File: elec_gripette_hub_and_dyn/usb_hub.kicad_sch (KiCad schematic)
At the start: 26 parts, among them J1 pico4, J3 Pogo-pin, J6 Pogo-pin, U1 FE1.1s_24-Pin_WQFN, U2 24C02S, Y1 12MHz

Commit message: [update] sch reviewed by Claude
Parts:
- added C21: 100n, Capacitor_SMD:C_0603_1608Metric, symbol Device:C_Small
- added D3: SP0503BAHT, Package_TO_SOT_SMD:SOT-143, symbol Power_Protection:SP0503BAHT
- J3, J6: footprint LCSC_parts_lib:SMD_BD1,2.0-L1.2-pogo-pin -> LCSC_parts_lib:CONN-TH_YZ95315064P-01_pogo; LCSC Part C5157386 -> C5157245
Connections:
- net +5V: now also C21.2
- net DM+: now also D3.3 (K)
- net DM-: now also D3.2 (K)
- net GND: now also C21.1, D3.1 (A)
- net at J1.2 (Pin_2), R2.1: now also D3.4 (K)
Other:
- note added: "(internaly generated by the USB hub)"

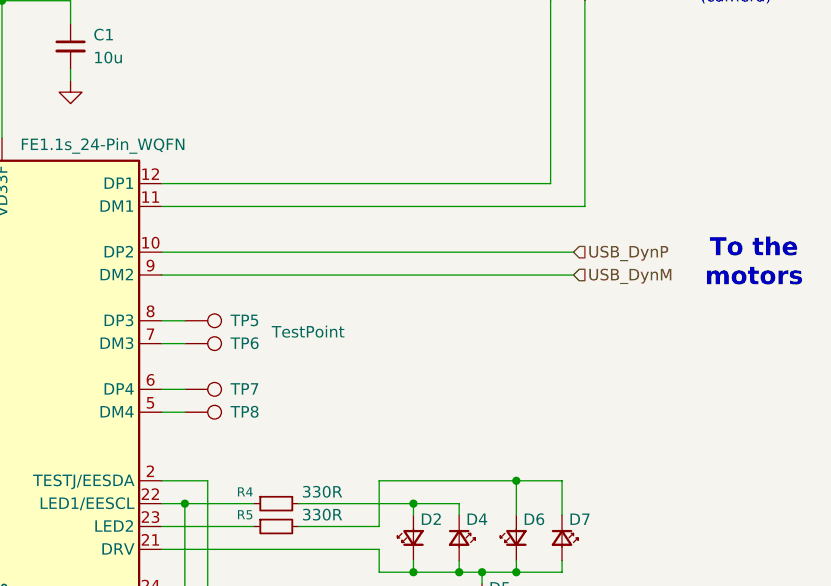
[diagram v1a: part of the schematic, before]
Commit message: [update] Gripette hub routed
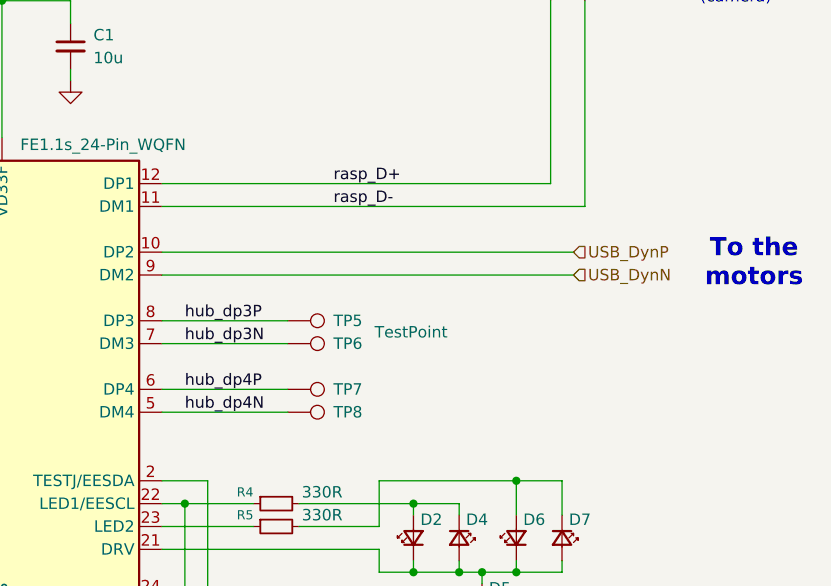
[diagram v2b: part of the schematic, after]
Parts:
- J1: footprint Connector_Molex:Molex_PicoBlade_53048-0410_1x04_P1.25mm_Horizontal -> Connector_Molex:Molex_PicoBlade_53047-0410_1x04_P1.25mm_Vertical; LCSC Part C588275 -> (none)
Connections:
- net rasp_D-: now reaches J6.1, U1.11 (DM1)
- net hub_dp4P: now reaches TP7.1, U1.6 (DP4)
- net hub_dp3N: now reaches TP6.1, U1.7 (DM3)
- net hub_dp4N: now reaches TP8.1, U1.5 (DM4)
- net hub_dp3P: now reaches TP5.1, U1.8 (DP3)
- net rasp_D+: now reaches J3.1, U1.12 (DP1)
- net USB_DynM renamed USB_DynN
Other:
- moved on the sheet: TP5, TP6, TP7, TP8
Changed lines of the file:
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@@
 	(wire
 		(pts
+			(xy 217.17 135.89) (xy 231.14 135.89)
+		)
+		(stroke
+			(width 0)
+			(type default)
+		)
+	)
+	(wire
+		(pts
 			(xy 219.71 200.66) (xy 219.71 146.05)
 		)
@@
 	(wire
 		(pts
-			(xy 130.81 125.73) (xy 130.81 130.81)
+			(xy 217.17 128.27) (xy 231.14 128.27)
 		)
 		(stroke
@@
 	(wire
 		(pts
-			(xy 256.54 152.4) (xy 256.54 153.67)
+			(xy 217.17 133.35) (xy 231.14 133.35)
 		)
 		(stroke
@@
 	(wire
 		(pts
-			(xy 217.17 146.05) (xy 219.71 146.05)
+			(xy 130.81 125.73) (xy 130.81 130.81)
 		)
 		(stroke
@@
 	(wire
 		(pts
-			(xy 260.35 90.17) (xy 260.35 110.49)
+			(xy 256.54 152.4) (xy 256.54 153.67)
 		)
 		(stroke
@@
 	(wire
 		(pts
-			(xy 130.81 125.73) (xy 130.81 115.57)
+			(xy 217.17 146.05) (xy 219.71 146.05)
 		)
 		(stroke
@@
 	(wire
 		(pts
-			(xy 170.18 97.79) (xy 170.18 96.52)
+			(xy 260.35 90.17) (xy 260.35 110.49)
 		)
 		(stroke
@@
 	(wire
 		(pts
-			(xy 179.07 163.83) (xy 179.07 165.1)
+			(xy 130.81 125.73) (xy 130.81 115.57)
 		)
 		(stroke
@@
 	(wire
 		(pts
-			(xy 219.71 133.35) (xy 217.17 133.35)
+			(xy 170.18 97.79) (xy 170.18 96.52)
 		)
 		(stroke
@@
 	(wire
 		(pts
-			(xy 250.19 153.67) (xy 252.73 153.67)
+			(xy 179.07 163.83) (xy 179.07 165.1)
 		)
 		(stroke
@@
 	(wire
 		(pts
-			(xy 245.11 146.05) (xy 245.11 147.32)
+			(xy 250.19 153.67) (xy 252.73 153.67)
 		)
 		(stroke
@@
 	(wire
 		(pts
-			(xy 232.41 146.05) (xy 245.11 146.05)
+			(xy 245.11 146.05) (xy 245.11 147.32)
 		)
 		(stroke
@@
 	(wire
 		(pts
-			(xy 245.11 203.2) (xy 237.49 203.2)
+			(xy 232.41 146.05) (xy 245.11 146.05)
 		)
 		(stroke
@@
 	(wire
 		(pts
-			(xy 194.31 90.17) (xy 194.31 105.41)
+			(xy 245.11 203.2) (xy 237.49 203.2)
 		)
 		(stroke
@@
 	(wire
 		(pts
-			(xy 128.27 118.11) (xy 181.61 118.11)
+			(xy 194.31 90.17) (xy 194.31 105.41)
 		)
 		(stroke
@@
 	(wire
 		(pts
-			(xy 252.73 166.37) (xy 252.73 167.64)
+			(xy 128.27 118.11) (xy 181.61 118.11)
 		)
 		(stroke
@@
 	(wire
 		(pts
-			(xy 241.3 153.67) (xy 245.11 153.67)
+			(xy 252.73 166.37) (xy 252.73 167.64)
 		)
 		(stroke
@@
 	(wire
 		(pts
-			(xy 219.71 135.89) (xy 217.17 135.89)
+			(xy 241.3 153.67) (xy 245.11 153.67)
 		)
 		(stroke
@@
 	(wire
 		(pts
-			(xy 219.71 128.27) (xy 217.17 128.27)
-		)
-		(stroke
-			(width 0)
-			(type default)
-		)
-	)
-	(wire
-		(pts
-			(xy 219.71 125.73) (xy 217.17 125.73)
+			(xy 217.17 125.73) (xy 231.14 125.73)
 		)
 		(stroke
@@
 		)
 	)
+	(label "rasp_D+"
+		(at 236.22 110.49 0)
+		(effects
+			(font
+				(size 1.27 1.27)
+			)
+			(justify left bottom)
+		)
+	)
+	(label "hub_dp3N"
+		(at 219.71 128.27 0)
+		(effects
+			(font
+				(size 1.27 1.27)
+			)
+			(justify left bottom)
+		)
+	)
+	(label "hub_dp4N"
+		(at 219.71 135.89 0)
+		(effects
+			(font
+				(size 1.27 1.27)
+			)
+			(justify left bottom)
+		)
+	)
 	(label "DM-"
 		(at 147.32 118.11 180)
@@
 		)
 	)
-	(hierarchical_label "USB_DynM"
+	(label "rasp_D-"
+		(at 236.22 113.03 0)
+		(effects
+			(font
+				(size 1.27 1.27)
+			)
+			(justify left bottom)
+		)
+	)
+	(label "hub_dp4P"
+		(at 219.71 133.35 0)
+		(effects
+			(font
+				(size 1.27 1.27)
+			)
+			(justify left bottom)
+		)
+	)
+	(label "hub_dp3P"
+		(at 219.71 125.73 0)
+		(effects
+			(font
+				(size 1.27 1.27)
+			)
+			(justify left bottom)
+		)
+	)
+	(hierarchical_label "USB_DynN"
 		(shape input)
 		(at 262.89 120.65 0)
@@
 			)
 		)
-		(property "Footprint" "Connector_Molex:Molex_PicoBlade_53048-0410_1x04_P1.25mm_Horizontal"
+		(property "Footprint" "Connector_Molex:Molex_PicoBlade_53047-0410_1x04_P1.25mm_Vertical"
 			(at 110.49 128.27 0)
 			(effects
@@
 			)
 		)
-		(property "LCSC Part" "C588275"
+		(property "LCSC Part" ""
 			(at 110.49 128.27 0)
 			(effects
@@
 	(symbol
 		(lib_id "Connector:TestPoint")
-		(at 219.71 133.35 270)
+		(at 231.14 133.35 270)
 		(unit 1)
 		(exclude_from_sim no)
@@
 		(fields_autoplaced yes)
 		(property "Reference" "TP7"
-			(at 224.79 133.3499 90)
+			(at 236.22 133.3499 90)
 			(effects
 				(font
@@
 		)
 		(property "Value" "TestPoint"
-			(at 224.79 134.6199 90)
+			(at 236.22 134.6199 90)
 			(effects
 				(font
@@
 		)
 		(property "Footprint" "TestPoint:TestPoint_Pad_D1.0mm"
-			(at 219.71 138.43 0)
+			(at 231.14 138.43 0)
 			(effects
 				(font
@@
 		)
 		(property "Datasheet" "~"
-			(at 219.71 138.43 0)
+			(at 231.14 138.43 0)
 			(effects
 				(font
@@
 		)
 		(property "Description" "test point"
-			(at 219.71 133.35 0)
+			(at 231.14 133.35 0)
 			(effects
 				(font
@@
 	(symbol
 		(lib_id "Connector:TestPoint")
-		(at 219.71 128.27 270)
+		(at 231.14 128.27 270)
 		(unit 1)
 		(exclude_from_sim no)
@@
 		(fields_autoplaced yes)
 		(property "Reference" "TP6"
-			(at 224.79 128.2699 90)
+			(at 236.22 128.2699 90)
 			(effects
 				(font
@@
 		)
 		(property "Value" "TestPoint"
-			(at 224.79 129.5399 90)
+			(at 236.22 129.5399 90)
 			(effects
 				(font
@@
 		)
 		(property "Footprint" "TestPoint:TestPoint_Pad_D1.0mm"
-			(at 219.71 133.35 0)
+			(at 231.14 133.35 0)
 			(effects
 				(font
@@
 		)
 		(property "Datasheet" "~"
-			(at 219.71 133.35 0)
+			(at 231.14 133.35 0)
 			(effects
 				(font
@@
 		)
 		(property "Description" "test point"
-			(at 219.71 128.27 0)
+			(at 231.14 128.27 0)
 			(effects
 				(font
@@
 	(symbol
 		(lib_id "Connector:TestPoint")
-		(at 219.71 135.89 270)
+		(at 231.14 135.89 270)
 		(unit 1)
 		(exclude_from_sim no)
@@
 		(fields_autoplaced yes)
 		(property "Reference" "TP8"
-			(at 224.79 135.8899 90)
+			(at 236.22 135.8899 90)
 			(effects
 				(font
@@
 		)
 		(property "Value" "TestPoint"
-			(at 224.79 137.1599 90)
+			(at 236.22 137.1599 90)
 			(effects
 				(font
@@
 		)
 		(property "Footprint" "TestPoint:TestPoint_Pad_D1.0mm"
-			(at 219.71 140.97 0)
+			(at 231.14 140.97 0)
 			(effects
 				(font
@@
 		)
 		(property "Datasheet" "~"
-			(at 219.71 140.97 0)
+			(at 231.14 140.97 0)
 			(effects
 				(font
@@
 		)
 		(property "Description" "test point"
-			(at 219.71 135.89 0)
+			(at 231.14 135.89 0)
 			(effects
 				(font
@@
 	(symbol
 		(lib_id "Connector:TestPoint")
-		(at 219.71 125.73 270)
+		(at 231.14 125.73 270)
 		(unit 1)
 		(exclude_from_sim no)
@@
 		(dnp no)
 		(property "Reference" "TP5"
-			(at 224.79 125.73 90)
+			(at 236.22 125.73 90)
 			(effects
 				(font
@@
 		)
 		(property "Value" "TestPoint"
-			(at 229.362 127 90)
+			(at 240.792 127 90)
 			(effects
 				(font
@@
 		)
 		(property "Footprint" "TestPoint:TestPoint_Pad_D1.0mm"
-			(at 219.71 130.81 0)
+			(at 231.14 130.81 0)
 			(effects
 				(font
@@
 		)
 		(property "Datasheet" "~"
-			(at 219.71 130.81 0)
+			(at 231.14 130.81 0)
 			(effects
 				(font
@@
 		)
 		(property "Description" "test point"
-			(at 219.71 125.73 0)
+			(at 231.14 125.73 0)
 			(effects
 				(font

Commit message: [uptate] Gripette hub ok for JLC
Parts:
- D2, D6: FT Rotation Offset (none) -> 180
- J1: FT Rotation Offset (none) -> 180; LCSC Part (none) -> C504989
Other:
- company: Pollen Robotics / Hugging Face -> Pollen Robotics/HF
- title: elec_maroilles -> Grippette - USB hub and Dynamixel device
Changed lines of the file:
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@@
 	(paper "A3")
 	(title_block
-		(title "elec_maroilles")
-		(date "2026-02-02")
-		(rev "B1")
-		(company "Pollen Robotics / Hugging Face")
+		(title "Grippette - USB hub and Dynamixel device")
+		(date "2026-04-16")
+		(rev "A1")
+		(company "Pollen Robotics/HF")
 	)
 	(text "To the\nmotors"
@@
 			)
 		)
-		(property "LCSC Part" ""
+		(property "LCSC Part" "C504989"
+			(at 110.49 128.27 0)
+			(effects
+				(font
+					(size 1.27 1.27)
+				)
+				(hide yes)
+			)
+		)
+		(property "FT Rotation Offset" "180"
 			(at 110.49 128.27 0)
 			(effects
@@
 			)
 		)
-		(property "FT Rotation Offset" ""
+		(property "FT Rotation Offset" "180"
 			(at 256.54 149.86 90)
 			(effects
@@
 			)
 		)
-		(property "FT Rotation Offset" ""
+		(property "FT Rotation Offset" "180"
 			(at 245.11 149.86 90)
 			(effects

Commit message: [update] Added error to gripette, going to B1
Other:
- note added: "hub active/suspend indicator"
- note added: "port 1 indicator"
- note added: "port 2 indicator"
- note added: "port 3 indicator"
- note added: "port 4 indicator"
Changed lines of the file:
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@@
+		)
+	)
+	(text "port 4 indicator"
+		(exclude_from_sim no)
+		(at 258.318 138.684 90)
+		(effects
+			(font
+				(size 1.27 1.27)
+			)
 		)
 	)
@@
 			)
 			(justify left)
+		)
+	)
+	(text "port 2 indicator"
+		(exclude_from_sim no)
+		(at 263.906 138.938 90)
+		(effects
+			(font
+				(size 1.27 1.27)
+			)
+		)
+	)
+	(text "port 3 indicator"
+		(exclude_from_sim no)
+		(at 246.888 138.176 90)
+		(effects
+			(font
+				(size 1.27 1.27)
+			)
 		)
 	)
@@
 		(effects
 			(font
+				(size 1.27 1.27)
+			)
+		)
+	)
+	(text "port 1 indicator"
+		(exclude_from_sim no)
+		(at 251.968 138.684 90)
+		(effects
+			(font
+				(size 1.27 1.27)
+			)
+		)
+	)
+	(text "hub active/suspend indicator"
+		(exclude_from_sim no)
+		(at 271.018 157.734 0)
+		(effects
+			(font

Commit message: [update] SCH B1-RC1
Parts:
- added C22: 100n, Capacitor_SMD:C_0603_1608Metric, symbol Device:C_Small
- added J10: Pogo-pin 2A, LCSC_parts_lib:CONN-TH_YZ08415060P-02_pogo, symbol Library_Pollen:pogo-pin
- added R23: DNP - 0R, Resistor_SMD:R_0402_1005Metric, symbol Device:R_Small
- D2, D6: FT Rotation Offset 180 -> (none); LCSC Part C19171301 -> C7429915
- D4, D7: LCSC Part C84263 -> C7429915
- D5: LCSC Part C7429915 -> C19171301
- J3, J6: value Pogo-pin -> Pogo-pin 4mm
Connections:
- net +3V3: now also C22.2
- net GND: now also C22.1
- net at R1.2, U1.16 (~{XRSTJ}): now also R23.1
- new net: J10.1, R23.2
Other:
- note added: "Reseting the hub from the rasp"
- moved on the sheet: C1

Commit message: [update] SCH + PCB B1-RC1
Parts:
- J10: value Pogo-pin 2A -> Pogo-pin 4mm; footprint LCSC_parts_lib:CONN-TH_YZ08415060P-02_pogo -> LCSC_parts_lib:CONN-TH_YZ95315064P-01_pogo; LCSC Part C7471674 -> C5157245
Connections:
- net DM+ renamed hub_DU+
- net DM- renamed hub_DU-
- net USB_DynN renamed hub_DP2-
- net USB_DynP renamed hub_DP2+
- net hub_dp3N renamed hub_DP3-
- net hub_dp3P renamed hub_DP3+
- net hub_dp4N renamed hub_DP4-
- net hub_dp4P renamed hub_DP4+
- net rasp_D+ renamed hub_DP1+
- net rasp_D- renamed hub_DP1-
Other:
- note added: "IO 17, H. pin 11"
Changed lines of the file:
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@@
 	(text "Reseting the hub\nfrom the rasp"
 		(exclude_from_sim no)
-		(at 147.066 78.486 0)
+		(at 147.066 72.644 0)
 		(effects
 			(font
@@
 		)
 	)
+	(text "IO 17, H. pin 11"
+		(exclude_from_sim no)
+		(at 147.066 77.47 0)
+		(effects
+			(font
+				(size 1.27 1.27)
+			)
+		)
+	)
 	(text "hub active/suspend indicator"
 		(exclude_from_sim no)
@@
 		)
 	)
-	(label "DM+"
+	(label "hub_DU+"
 		(at 143.51 115.57 180)
 		(effects
@@
 		)
 	)
-	(label "rasp_D+"
+	(label "hub_DP1+"
 		(at 236.22 110.49 0)
 		(effects
@@
 		)
 	)
-	(label "hub_dp3N"
+	(label "hub_DP3-"
 		(at 219.71 128.27 0)
 		(effects
@@
 		)
 	)
-	(label "hub_dp4N"
+	(label "hub_DP4-"
 		(at 219.71 135.89 0)
 		(effects
@@
 		)
 	)
-	(label "DM-"
+	(label "hub_DU-"
 		(at 143.51 118.11 180)
 		(effects
@@
 		)
 	)
-	(label "rasp_D-"
+	(label "hub_DP1-"
 		(at 236.22 113.03 0)
 		(effects
@@
 		)
 	)
-	(label "hub_dp4P"
+	(label "hub_DP4+"
 		(at 219.71 133.35 0)
 		(effects
@@
 		)
 	)
-	(label "hub_dp3P"
+	(label "hub_DP3+"
 		(at 219.71 125.73 0)
 		(effects
@@
 		)
 	)
-	(hierarchical_label "USB_DynN"
+	(hierarchical_label "hub_DP2-"
 		(shape input)
 		(at 262.89 120.65 0)
@@
 		)
 	)
-	(hierarchical_label "USB_DynP"
+	(hierarchical_label "hub_DP2+"
 		(shape input)
 		(at 262.89 118.11 0)
@@
 			)
 		)
-		(property "Value" "Pogo-pin 2A"
+		(property "Value" "Pogo-pin 4mm"
 			(at 144.78 88.6632 90)
 			(effects
@@
 			)
 		)
-		(property "Footprint" "LCSC_parts_lib:CONN-TH_YZ08415060P-02_pogo"
+		(property "Footprint" "LCSC_parts_lib:CONN-TH_YZ95315064P-01_pogo"
 			(at 147.32 93.98 0)
 			(effects
@@
 			)
 		)
-		(property "LCSC Part" "C7471674"
+		(property "LCSC Part" "C5157245"
 			(at 147.32 93.98 90)
 			(effects

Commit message: [update] Before review
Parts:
- R23: value DNP - 0R -> DNP-0R; footprint Resistor_SMD:R_0402_1005Metric -> Resistor_SMD:R_0603_1608Metric; LCSC Part C17168 -> (none)
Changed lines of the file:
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@@
 			)
 		)
-		(property "Value" "DNP - 0R"
+		(property "Value" "DNP-0R"
 			(at 149.86 103.124 90)
 			(effects
@@
 			)
 		)
-		(property "Footprint" "Resistor_SMD:R_0402_1005Metric"
+		(property "Footprint" "Resistor_SMD:R_0603_1608Metric"
 			(at 147.32 102.87 0)
 			(effects
@@
 			)
 		)
-		(property "LCSC Part" "C17168"
+		(property "LCSC Part" ""
 			(at 147.32 102.87 90)
 			(effects

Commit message: [update] review by Claude. Corrections, RC2
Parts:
- added R41: 0R, Resistor_SMD:R_0402_1005Metric, symbol Device:R_Small
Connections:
- net +5V: no longer C2.2, R6.1, R7.1, R8.2, U1.17 (VBUSM), U2.4 (Vcc)
- net at D3.4 (K), J1.2 (Pin_2), R2.1: now also R41.1
- net +3V3 renamed VPP
- net VPP: now also C2.2, R6.1, R7.1, R8.2, U2.4 (Vcc)
- new net: R41.2, U1.17 (VBUSM)
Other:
- note added: "(3V3 internaly generated by the USB hub)"
- note removed: "(internaly generated by the USB hub)"
